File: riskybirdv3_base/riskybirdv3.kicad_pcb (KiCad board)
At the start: 4 copper layers, 70 x 70.6 mm, 182 parts, among them IC1 PMW3901MB-TXQT, J1 Conn_02x10_Odd_Even, J10 Conn_01x05, J11 Conn_01x05, J12 Conn_01x02, J2 Conn_01x05, J3 Conn_01x02, J4 Conn_01x02, J5 Conn_01x02, J6 Conn_01x02, J8 USB_C_Receptacle_USB2.0_16P, J9 Conn_01x05, Q1 SI2302, Q2 SI2302, Q3 SI2302, Q4 SI2302, Q5 AON7407, Q6 2N7002, Q7 2N7002, Q9 AON7534, SW1 SW_SPST, SW2 SW_SPST, SW4 SW_SPST, SW5 SW_SPST, U1 ADS7128IRTER, U10 TLV70018DCKR, U11 TLV70015DCKT, U12 PCA9306DC, U13 LM74700, U14 ESP32-C6-MINI-1/U, U2 LTC3119EUFD#TRPBF, U3 BMI088, U4 MCP73831-2-OT, U5 BMP390, U6 USBLC6-2P6, U7 TLV70028DCKR, U8 LM66100DCK, U9 VL53L1CXV0FY1

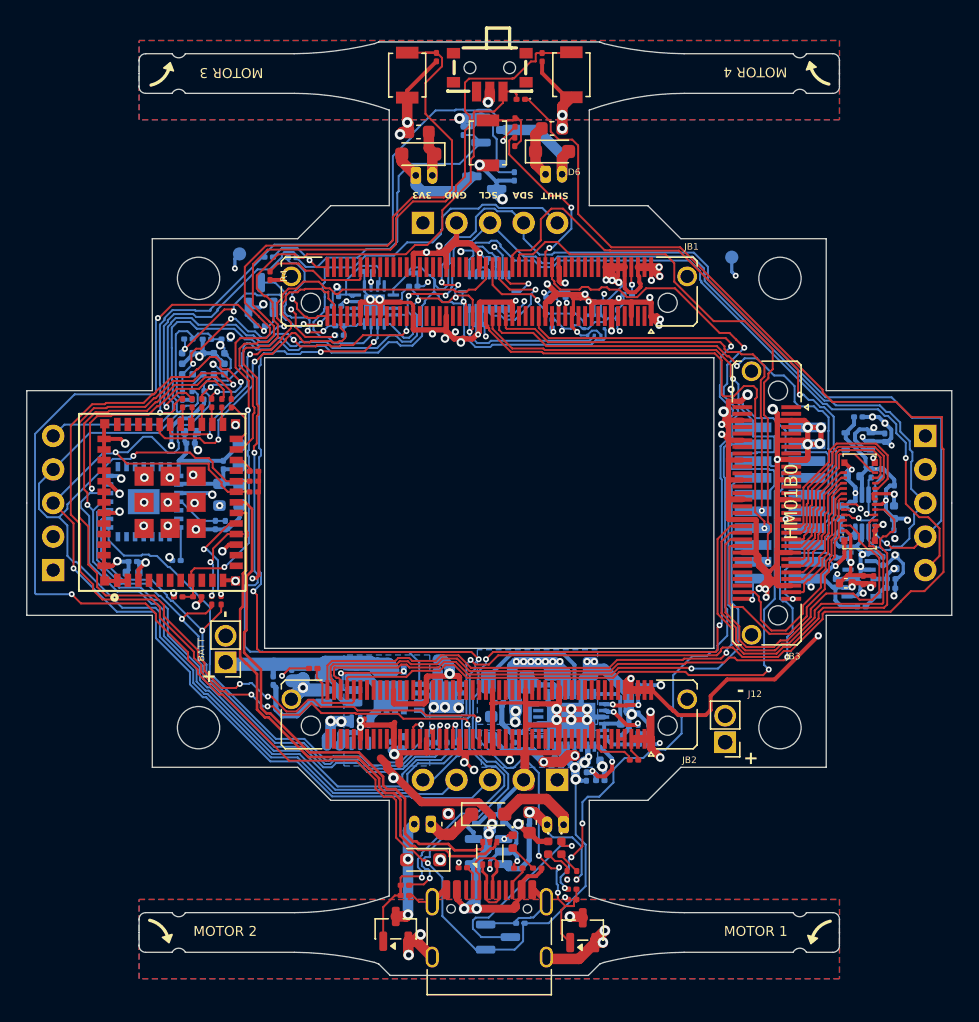
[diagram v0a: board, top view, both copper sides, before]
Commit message: riskybirdv3: single-rail 3v3 redesign (TPS552882 + TPS25982 eFuse); layout = JB1.13 short-fix only
Checkpoint before layout rework. Schematic carries the full new power rail;
the PCB has ONLY the JB1.13 short fix (no new-rail placement/routing yet).

Schematic:
- New single 3.3V buck-boost rail replaces the old LTC3119 stage:
  U15 = TPS552882QRPMRQ1 (buck-boost, ext buck FETs Q8/Q10 AON7534),
  L1 = SRP1265A-2R2M (2.2uH), FB 100k/56.2k=3.34V, ILIM 27k=12.2A,
  FSW 28.7k=~690kHz, MODE 27k=PFM+internal-LDO, COMP 2.6k/8.2n/100p,
  EN/UVLO 40.2k/28k=3.0V, AGND single-point tie via net-tie NT1.
- Input eFuse U16 = TPS259824ONRGER on VSYS->VSYS_FUSED:
  ILIM 121R=12.2A, ITIMER 22n=~178us, dVdt 150p, IMON 604R,
  RETRY_DLY/NRETRY/LDSTRT=GND (latch-off), PG->/FUSE_PG,
  EN via SW5 + 60.4k/40.2k divider = 3.0V UVLO.
- Removed old LTC3119 rail: U2 + Q5 load switch + VCOM node + associated
  passives (L4, FB/RT/RUN/comp/BST, VCOM caps).
- SW5 master switch moved from Q5 gate to the eFuse EN; Q6/Q7 re-gated from
  VCOM to /FUSE_PG (system-on).
- BMP390 -> BMP388 (C779278, same LGA-10); PMW3901 DNP cleared + LCSC C43496881.

Layout (riskybirdv3.kicad_pcb): JB1.13 GND->+3V3 short fix only (pad-13
removed); BMP388/PMW3901 property updates. New power-rail components not yet
placed/routed.

Libraries: imported to riskybird_lcsc - TPS552882QRPMRQ1, TPS259824ONRGER,
SRP1265A-2R2M, MWSA1204S-1R0MT (+ footprints/3D).
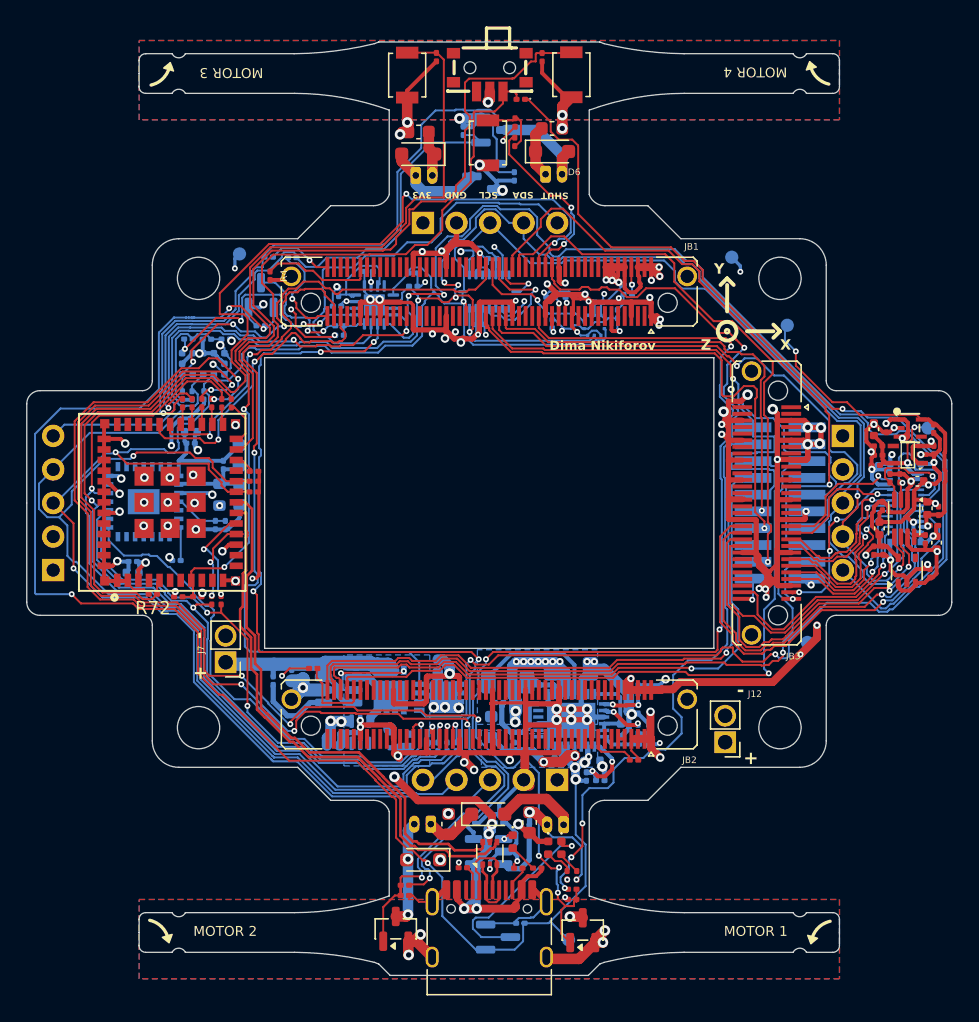
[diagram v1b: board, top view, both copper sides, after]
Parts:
- removed the G*** at (142.8, 106.0)
- added 1V5: TestPoint, TestPoint:TestPoint_Pad_D1.0mm, B.Cu at (133.2, 94.3)
- added 1V8: TestPoint, TestPoint:TestPoint_Pad_D1.0mm, B.Cu at (124.1, 110.5)
- added 2V8: TestPoint, TestPoint:TestPoint_Pad_D1.0mm, B.Cu at (122.5, 86.5)
- added R72: 10k, Resistor_SMD:R_0201_0603Metric, F.Cu at (74.5, 106.9)
- added TP1: TestPoint, TestPoint:TestPoint_Pad_D1.0mm, B.Cu at (106.0, 133.1)
- added TP2: TestPoint, TestPoint:TestPoint_Pad_D1.0mm, B.Cu at (92.5, 117.1)
- C42, C51, C52, C55, C57, C59, C66, C68, C69, C70, C71, C72, C73, C74, R67, R68, R69, U10, U11, U12, U7: moved to F.Cu
- HM01B0: footprint riskybird_lcsc:CONN-SMD_24P-P0.40_5055502420 -> riskybird_lcsc:CONN-SMD_24P-P0.40_5055502420-HM01B0; moved to B.Cu
- U5: value BMP390 -> BMP388
- moved C70 12.5 mm to (133.7, 96.0)
- moved C59 12.5 mm to (133.6, 94.4)
- moved C68 10.8 mm to (133.3, 105.3), turned to -90 degrees
- moved U7 10.8 mm to (131.9, 94.3)
- moved C66 10.8 mm to (129.2, 97.2)
- moved U11 10.7 mm to (131.7, 96.3), turned to 0 degrees
- moved U10 10.4 mm to (131.6, 105.1), turned to 90 degrees
- moved C42 10.3 mm to (129.8, 103.6), turned to -90 degrees
- moved C74 10.2 mm to (129.1, 94.4)
- moved C55 10.1 mm to (129.4, 95.7), turned to 180 degrees
- moved C57 10.1 mm to (129.4, 96.4), turned to 180 degrees
- moved C69 10.1 mm to (130.1, 94.3)
- moved C75 8.38 mm to (133.2, 100.4), turned to -90 degrees
- moved C54 7.74 mm to (134.0, 100.6), turned to 90 degrees
- moved C71 7.60 mm to (133.8, 103.0)
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- renumbered BATT to BATT1, BATT to J7
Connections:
- net /VSYS renamed VSYS
- JB1 pad 13: GND -> +3V3
- JB1 pad 36: unconnected-(JB1-Pin_36-Pad36) -> /ESP_RESET
- JB3 pad 37: /D0 -> /MCLK
- JB3 pad 38: /INT -> /TRIG
- JB3 pad 39: /D2 -> /D0
- JB3 pad 41: /D4 -> /D1
- JB3 pad 42: /TRIG -> /LVLD
- JB3 pad 43: /D6 -> /D2
- JB3 pad 44: /LVLD -> /INT
- JB3 pad 47: /D7 -> /D3
- JB3 pad 49: /D5 -> /D4
- JB3 pad 51: /D3 -> /D5
- JB3 pad 53: /D1 -> /D6
- JB3 pad 58: /MCLK -> /D7
- U14 pad 5: unconnected-(U14-GPIO2/ADC1_CH2-Pad5) -> /ESP_RESET
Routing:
- net /ESP_RESET: track 0.00 -> 80.0 mm, vias 0 -> 2
- net +2V8: track 8.41 -> 25.2 mm, vias 1 -> 2
- net /GPIO2: track 66.2 -> 80.5 mm, vias 3 -> 2
- net +1V8: track 93.4 -> 83.5 mm, vias 5 -> 6
- net /LVLD: track 21.5 -> 31.4 mm, vias 0 -> 1
- net GND: track 530.6 -> 521.3 mm, vias 112 -> 108
- net /D7: track 9.03 -> 17.6 mm, vias 0 -> 1
- net /PCLK: track 9.99 -> 18.3 mm, vias 0 -> 3
- net /MCLK: track 17.5 -> 10.1 mm, vias 0 -> 1
- net /CAM_SCL: track 3.42 -> 10.6 mm
- net /D0: track 15.5 -> 9.84 mm, vias 0 -> 1
- net /INT: track 33.7 -> 28.2 mm, vias 0 -> 1
- net /TRIG: track 28.8 -> 33.2 mm, vias 0 -> 1
- net /D3: track 9.22 -> 13.5 mm, vias 0 -> 1
- net /D2: track 14.8 -> 11.1 mm, vias 0 -> 1
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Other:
- outline, holes or cut-outs redrawn
- board text added: "Dima Nikiforov"
- board text added: "VCOM"
- board text added: "VSYS"
- board text added: "X"
- board text added: "Y"
- board text added: "Z"

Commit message: riskybirdv3: annotate missing LCSC parts (sch) + PCB F8 net update / J1-J2 ECO
Schematic: assigned LCSC Part to the 47 in-BOM parts that had none
(caps, LEDs, BAT54, 1x05 headers, SI2302/2N7002 FETs, R25, and
U1/U3/U6/U8/U9/U10/U12/U13) — values per docs/RESPIN_BOM_JLC.md.
Electrically neutral: the 185 electrical ERC violations are unchanged.
J7/J12 left as in_bom=no solder-pad connectors (battery lead / PSU override).

Board: F8 net update from the completed single-rail power routing, plus
J1/J2 footprint ECO tweaks. Footprint LCSC bindings are NOT yet synced
from the schematic (F8 was run with "don't overwrite footprints"), so the
PCB footprints still lack LCSC on those 47 + R35 — to be applied in a
follow-up direct patch that preserves the J1/J2 footprint edits.
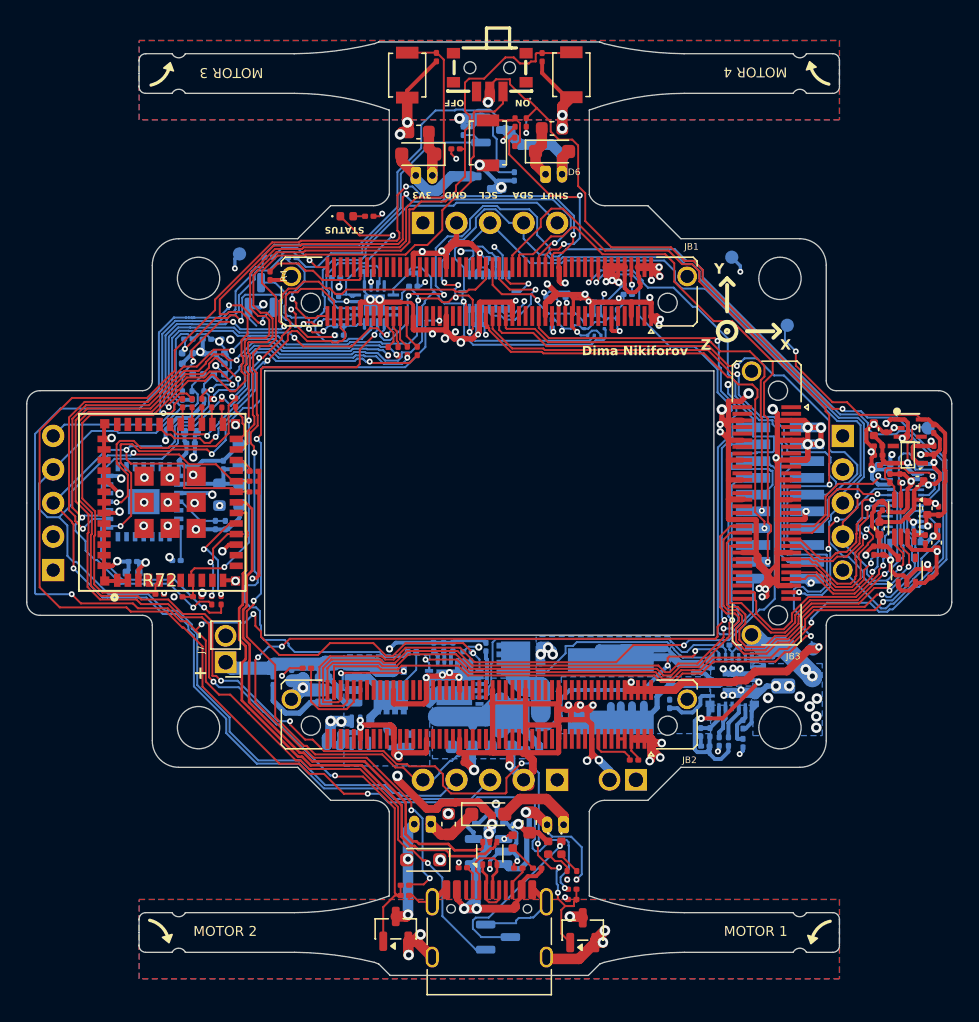
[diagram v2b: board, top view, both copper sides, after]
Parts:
- removed C60, C61: 0.1u, Capacitor_SMD:C_0201_0603Metric
- removed C62, C67: 10u, Capacitor_SMD:C_0402_1005Metric
- removed C63: 150u, Capacitor_SMD:C_1206_3216Metric
- removed C64: 470p, Capacitor_SMD:C_0201_0603Metric
- removed C65: 4.7u, Capacitor_SMD:C_0402_1005Metric
- removed L4: 2.2u, Inductor_SMD:L_0603_1608Metric
- removed Q5: AON7407, riskybird_lcsc:DFN-8_L3.0-W3.0-P0.65-BL
- removed R47, R48: 200k, Resistor_SMD:R_0201_0603Metric
- removed R59: 316k, Resistor_SMD:R_0201_0603Metric
- removed R60: 100k, Resistor_SMD:R_0201_0603Metric
- removed R61: 52.3k, Resistor_SMD:R_0201_0603Metric
- removed R62: 48.7k, Resistor_SMD:R_0201_0603Metric
- removed R70: 0R, Resistor_SMD:R_1206_3216Metric
- removed R71: 63k, Resistor_SMD:R_0201_0603Metric
- removed TP1: TestPoint, TestPoint:TestPoint_Pad_D1.0mm
- removed U2: LTC3119EUFD#TRPBF, riskybird_lcsc:QFN-28_L5.0-W4.0-P0.50-TL-EP
- added C76: 0.1u, Capacitor_SMD:C_0201_0603Metric, B.Cu at (113.7, 115.2)
- added C78: 0.1u, Capacitor_SMD:C_0201_0603Metric, B.Cu at (115.5, 112.5)
- added C79: 4.7uF, Capacitor_SMD:C_0201_0603Metric, B.Cu at (116.4, 116.3)
- added C80: 150u, Capacitor_SMD:C_1206_3216Metric, B.Cu at (122.2, 112.4)
- added C81: 82p, Capacitor_SMD:C_0201_0603Metric, B.Cu at (116.7, 117.3)
- added C82: 5.6n, Capacitor_SMD:C_0201_0603Metric, B.Cu at (116.3, 118.4)
- added C83: 150p, Capacitor_SMD:C_0201_0603Metric, B.Cu at (99.8, 110.9)
- added C84: 22n, Capacitor_SMD:C_0201_0603Metric, B.Cu at (95.8, 110.9)
- added C85: 10u, Capacitor_SMD:C_0402_1005Metric, B.Cu at (103.3, 118.7)
- added C86: 22u, Capacitor_SMD:C_0603_1608Metric, B.Cu at (100.9, 118.5)
- added C87: 22u, Capacitor_SMD:C_0603_1608Metric, B.Cu at (97.9, 118.5)
- added D8: LED, LED_SMD:LED_0402_1005Metric, F.Cu at (89.2, 78.3)
- added L2: XAL7030-152MEC, riskybird_lcsc:IND-SMD_L7.5-W7.5_XAL7030-152MEC, B.Cu at (109.2, 114.2)
- added Q10: AON7534, riskybird_lcsc:PQFN-8_L3.1-W3.1-P0.65-LS3.3-BL, B.Cu at (102.4, 111.8)
- added Q8: AON7534, riskybird_lcsc:PQFN-8_L3.1-W3.1-P0.65-LS3.3-BL, B.Cu at (102.3, 116.1)
- added R35: 150, Resistor_SMD:R_0201_0603Metric, F.Cu at (90.9, 78.3)
- added R49: 121, Resistor_SMD:R_0201_0603Metric, B.Cu at (96.5, 110.9)
- added R50: 604, Resistor_SMD:R_0201_0603Metric, B.Cu at (97.2, 110.9)
- added R51: 100k, Resistor_SMD:R_0201_0603Metric, B.Cu at (98.3, 111.2)
- added R52: 60.4k, Resistor_SMD:R_0201_0603Metric, B.Cu at (94.2, 111.2)
- added R73: 100k, Resistor_SMD:R_0201_0603Metric, B.Cu at (119.2, 116.8)
- added R74: 56.2k, Resistor_SMD:R_0201_0603Metric, B.Cu at (119.2, 118.2)
- added R75: 27k, Resistor_SMD:R_0201_0603Metric, B.Cu at (117.4, 118.0)
- added R76: 19.6k, Resistor_SMD:R_0201_0603Metric, B.Cu at (120.8, 112.0)
- added R77: 27k, Resistor_SMD:R_0201_0603Metric, B.Cu at (118.1, 118.0)
- added R78: 40.2k, Resistor_SMD:R_0201_0603Metric, B.Cu at (117.8, 110.8)
- added R79: 3.65k, Resistor_SMD:R_0201_0603Metric, B.Cu at (116.0, 117.3)
- added R80: 28k, Resistor_SMD:R_0201_0603Metric, B.Cu at (119.3, 111.0)
- added TP3: TestPoint, TestPoint:TestPoint_Pad_D1.0mm, B.Cu at (98.8, 116.8)
- added U15: TPS552882QRPMRQ1, riskybird_lcsc:VQFN-HR-26_L4.0-W3.5_TPS55288RPMR, B.Cu at (118.4, 113.5)
- added U16: TPS259824ONRGER, riskybird_lcsc:VQFN-24_L4.0-W4.0-P0.50-TL-EP_TI_RGE, B.Cu at (97.3, 114.0)
- FID1: value DroneFrame -> Fiducial
- J12: moved to B.Cu
- R27, R28, R29, R34: moved to F.Cu
- R45: value 100k -> 40.2k
- R58: value 100k -> 10k; moved to F.Cu
- moved R58 48.5 mm to (97.5, 73.2), turned to 0 degrees
- moved G1 43.4 mm to (89.5, 80.8), turned to 0 degrees
- moved R28 30.1 mm to (93.8, 88.5)
- moved R27 30.1 mm to (94.5, 88.5)
- moved R34 30.1 mm to (92.3, 88.5)
- moved R29 30.1 mm to (93.1, 88.5)
- moved J12 7.33 mm to (111.1, 121.0), turned to 90 degrees
- moved C6 2.15 mm to (88.4, 83.0), turned to 0 degrees
- moved R45 1.80 mm to (102.8, 71.2), turned to 90 degrees
- moved 1V8 0.66 mm to (124.5, 111.0)
- moved R72 0.51 mm to (75.1, 106.9), turned to 0 degrees
- moved R39 0.49 mm to (86.2, 112.5)
- moved R63 0.32 mm to (80.8, 92.4)
- moved G*** 0.11 mm to (118.2, 86.0)
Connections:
- JB1 pad 18: unconnected-(JB1-Pin_18-Pad18) -> /TSI_UART_RX
- JB1 pad 20: unconnected-(JB1-Pin_20-Pad20) -> /TSI_UART_TX
- JB1 pad 65: unconnected-(JB1-Pin_65-Pad65) -> /MOTION
- JB1 pad 75: unconnected-(JB1-Pin_75-Pad75) -> Net-(JB1-Pin_75-Pad75)
- JB1 pad 77: unconnected-(JB1-Pin_77-Pad77) -> Net-(JB1-Pin_77-Pad77)
- JB1 pad 79: unconnected-(JB1-Pin_79-Pad79) -> Net-(JB1-Pin_79-Pad79)
- JB1 pad 81: unconnected-(JB1-Pin_61-Pad81) -> Net-(JB1-Pin_61-Pad81)
- JB2 pad 61: Net-(JB2-Pin_61-Pad61) -> unconnected-(JB2-Pin_61-Pad61)
- JB2 pad 63: Net-(JB2-Pin_63-Pad63) -> unconnected-(JB2-Pin_63-Pad63)
- JB2 pad 65: Net-(JB2-Pin_65-Pad65) -> unconnected-(JB2-Pin_65-Pad65)
- JB2 pad 67: Net-(JB2-Pin_67-Pad67) -> unconnected-(JB2-Pin_67-Pad67)
- JB2 pad 73: /MOTION -> unconnected-(JB2-Pin_73-Pad73)
- JB3 pad 59: /TSI_UART_TX -> unconnected-(JB3-Pin_59-Pad59)
- JB3 pad 60: /TSI_UART_RX -> unconnected-(JB3-Pin_60-Pad60)
- Q6 pad 1: VCOM -> /FUSE_PG
- Q7 pad 1: VCOM -> /FUSE_PG
- R27 pad 1: Net-(JB2-Pin_61-Pad61) -> Net-(JB1-Pin_75-Pad75)
- R28 pad 1: Net-(JB2-Pin_63-Pad63) -> Net-(JB1-Pin_77-Pad77)
- R29 pad 1: Net-(JB2-Pin_65-Pad65) -> Net-(JB1-Pin_79-Pad79)
- R29 pad 2: /SCLK -> /MOSI
- R34 pad 1: Net-(JB2-Pin_67-Pad67) -> Net-(JB1-Pin_61-Pad81)
- R34 pad 2: /MOSI -> /SCLK
- R45 pad 1: Net-(Q5-G) -> GND
- R45 pad 2: VSYS -> Net-(SW5-B)
- R58 pad 1: VCOM -> +3V3
- R58 pad 2: Net-(U2-RUN) -> /GPIO9
- SW5 pad 1: Net-(Q5-G) -> Net-(SW5-A)
- SW5 pad 2: GND -> Net-(SW5-B)
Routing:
- net VCOM: track 160.3 -> 0.00 mm, vias 11 -> 0
- net /FUSE_PG: track 0.00 -> 115.1 mm, vias 0 -> 7
- net Net-(SW5-B): track 0.00 -> 106.7 mm, vias 0 -> 4
- net VSYS: track 108.9 -> 15.5 mm, vias 3 -> 0
- net Net-(Q5-G): track 77.6 -> 0.00 mm, vias 1 -> 0
- net Net-(SW5-A): track 0.00 -> 71.6 mm, vias 0 -> 1
- net Net-(JB1-Pin_32): track 70.6 -> 126.6 mm
- net /TSI_UART_RX: track 1.62 -> 41.9 mm
- net VSYS_FUSED: track 0.00 -> 34.5 mm
- net Net-(U15-SW1): track 0.00 -> 32.4 mm
- net /TSI_UART_TX: track 3.41 -> 35.3 mm
- net /NCS: track 63.3 -> 32.8 mm, vias 1 -> 2
- net /MISO: track 62.8 -> 35.2 mm, vias 1 -> 3
- net Net-(C76-Pad2): track 0.00 -> 22.7 mm
- net Net-(JB1-Pin_35): track 82.2 -> 100.6 mm, vias 4 -> 6
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- added copper zone on B.Cu, net +3V3
- added copper zone on B.Cu, net Net-(C76-Pad2)
- added copper zone on B.Cu, net Net-(U15-SW1)
- added copper zone on B.Cu, net VSYS_FUSED
- removed copper zone on B.Cu, net Net-(C60-Pad2)
- removed copper zone on B.Cu, net Net-(C61-Pad2)
- removed copper zone on B.Cu, net Net-(U2-BST1)
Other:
- board text added: "OFF"
- board text added: "ON"
- board text added: "STATUS"
- board text added: "V3.1"
- board text added: "VSYS_F"
- board text removed: "V3"

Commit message: riskybirdv3: correct power-rail passive BOM + cap voltage uprate + AGND net-tie
Fixes a systemic copy-paste mis-annotation where 16 power-rail passives carried
the wrong LCSC/MPN (Value edited, part field left pointing at the source part).
Built as-is, JLC would have placed 100k for every set-point resistor and
1uF/100nF for the COMP + eFuse timing caps -> dead rail. Each now has the
correct part:
  R45/R78=40.2k C423536, R49=121 C474519, R50=604 C423470, R52=60.4k C473653,
  R74=57.6k C320974, R75/R77=27k C273283, R76=19.6k C423675, R79=3.65k C166220,
  R80=28k C473489, C81=82p C161439, C82=5.6n C3037635, C83=150p C384963,
  C84=22n C2880350.

Design edits from docs/RESPIN_POWER_VERIFY.md:
- R74 56.2k->57.6k: Vout 3.335->3.283V (whole band under TE0841 3.4V abs-max).
- VSYS/VSYS_FUSED Cin voltage uprate: C86/C87 22uF 6.3V->16V (C6119868),
  C49 10uF 0402 6.3V -> 10uF/16V 0603 (C962136, footprint resized+rerouted),
  C85 10uF 6.3V -> 4.7uF/25V 0402 (C2858031).
- C79 relabeled 4.7uF->1uF to match the accepted 1uF part (C53067).

Also: added the missing AGND<->GND net-tie footprint (NT1); synced all LCSC
bindings schematic->PCB footprints (48 added incl. R35, 15 updated),
J1/J2 footprints preserved.

Electrically neutral (185 ERC electrical violations unchanged); 0 value<->LCSC
mismatches; 0 in-BOM footprints missing LCSC.
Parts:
- added NT1: NetTie_2, NetTie:NetTie-2_SMD_Pad0.5mm, B.Cu at (115.0, 118.2)
- added TP4: TestPoint, TestPoint:TestPoint_Pad_D1.0mm, B.Cu at (111.5, 79.2)
- C49: value 10u -> 10u/16V; footprint Capacitor_SMD:C_0402_1005Metric -> Capacitor_SMD:C_0603_1608Metric
- C79: value 4.7uF -> 1u
- C85: value 10u -> 4.7u/25V
- C86, C87: value 22u -> 22u/16V
- R74: value 56.2k -> 57.6k
- moved C49 0.46 mm to (94.3, 117.7)
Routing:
- net GND: track 515.0 -> 517.9 mm, vias 118 -> 121
